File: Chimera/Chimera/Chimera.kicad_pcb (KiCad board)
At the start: 4 copper layers, 72 x 41.5 mm, 110 parts, among them J1 Fork 1, J10 DM3CS-SF, J2 Fork 2, J3 Flamethrower, J4 Therm 1, J5 Therm 2, J6 Therm 3, J7 Therm 4, J8 Button, J9 USB_B_Micro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

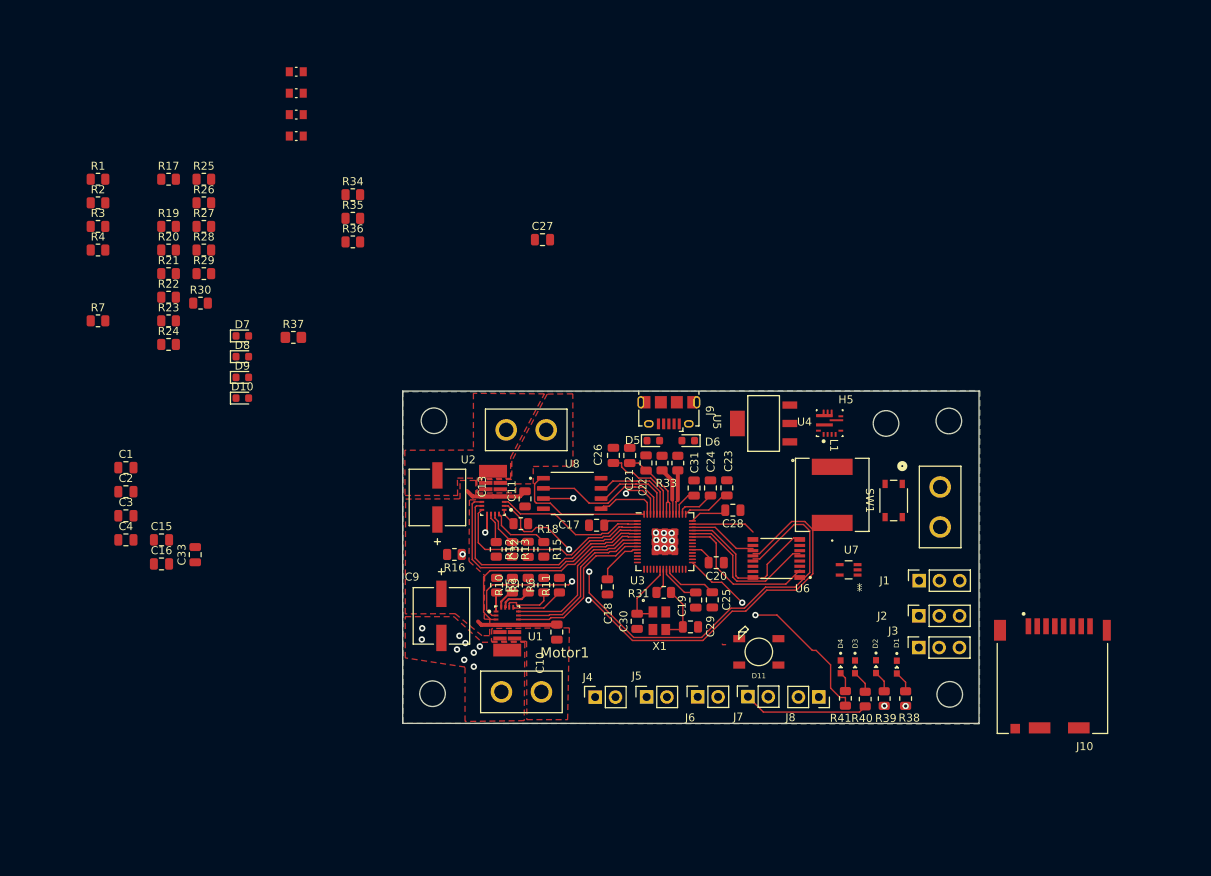
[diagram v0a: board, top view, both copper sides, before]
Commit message: Rewiring M2 and moved Debugging LEDS
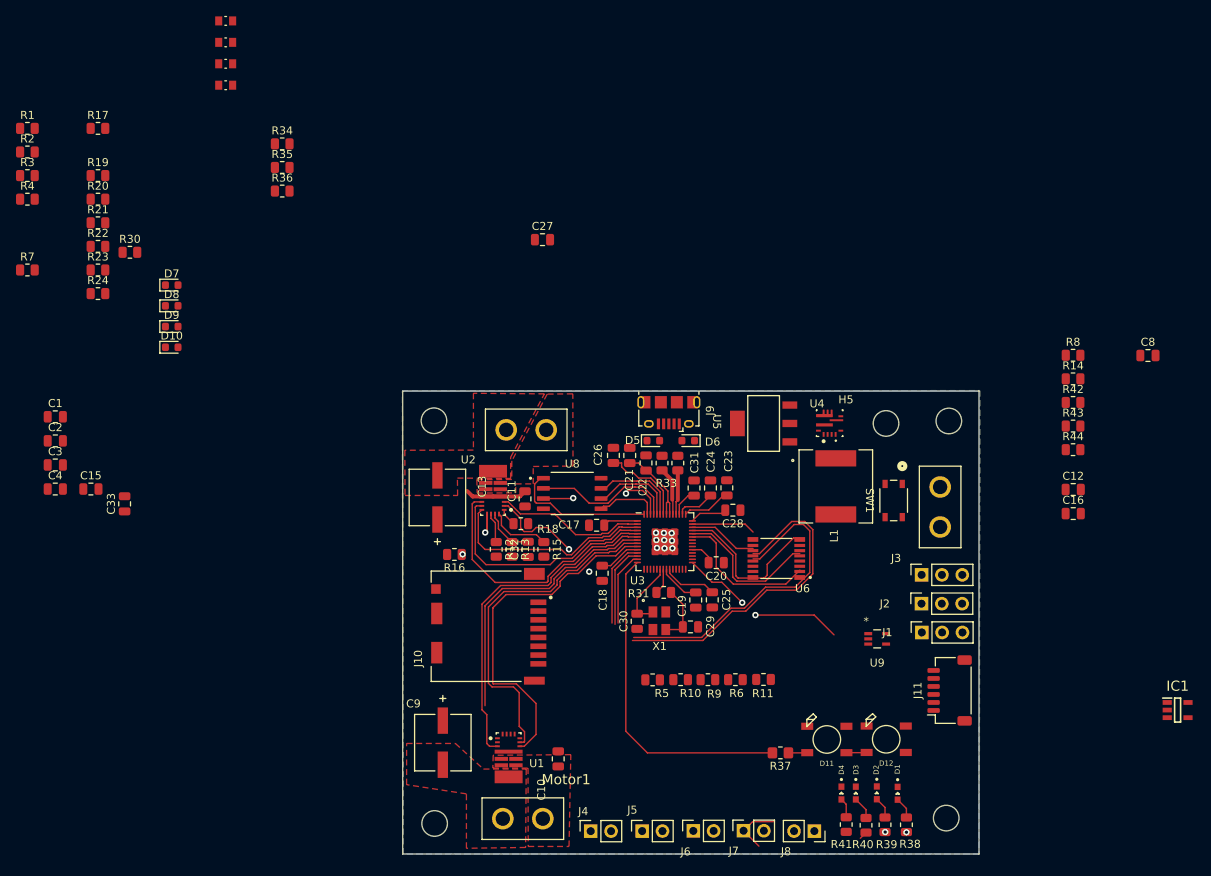
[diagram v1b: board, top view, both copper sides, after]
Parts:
- removed R25: 100m, Resistor_SMD:R_0805_2012Metric
- removed R26, R27: 10k, Resistor_SMD:R_0805_2012Metric
- removed R28, R29: 500k, Resistor_SMD:R_0805_2012Metric
- removed U7: OpAmp, chimera:SC70-5_LT_MCH-M
- added C12: 1uF, Capacitor_SMD:C_0805_2012Metric, F.Cu at (155.7, 74.0)
- added C8: .1uF, Capacitor_SMD:C_0805_2012Metric, F.Cu at (165.0, 57.3)
- added D12: NeoPixel_THT, chimera:WS2812B, F.Cu at (132.3, 105.2)
- added IC1: AP7375-50W5-7, chimera:SOT95P285X140-5N, F.Cu at (168.7, 101.6)
- added J11: Reciver, Connector_JST:JST_SH_SM06B-SRSS-TB_1x06-1MP_P1.00mm_Horizontal, F.Cu at (140.2, 99.1)
- added R14: 10k, Resistor_SMD:R_0805_2012Metric, F.Cu at (155.7, 60.2)
- added R42: 10k, Resistor_SMD:R_0805_2012Metric, F.Cu at (155.7, 63.1)
- added R43: 500k, Resistor_SMD:R_0805_2012Metric, F.Cu at (155.7, 66.1)
- added R44: 500k, Resistor_SMD:R_0805_2012Metric, F.Cu at (155.7, 69.0)
- added R8: 100m, Resistor_SMD:R_0805_2012Metric, F.Cu at (155.7, 57.2)
- added U9: OpAmp, chimera:SC70-5_LT_MCH-M, F.Cu at (131.2, 92.7)
- C16: value .1uF -> 10uF
- moved C16 114.1 mm to (155.7, 77.0)
- moved R37 80.0 mm to (119.1, 106.9), turned to 180 degrees
- moved J10 71.1 mm to (82.5, 91.3), turned to 90 degrees
- moved R11 28.1 mm to (117.0, 97.8), turned to 0 degrees
- moved R6 26.7 mm to (113.5, 97.8), turned to 0 degrees
- moved R9 25.4 mm to (110.0, 97.8), turned to 0 degrees
- moved R10 24.1 mm to (106.6, 97.8), turned to 0 degrees
- moved R5 22.8 mm to (103.1, 97.8), turned to 0 degrees
- moved J4 16.8 mm to (95.4, 116.7)
- moved J5 16.8 mm to (101.8, 116.7)
- moved J6 16.8 mm to (108.2, 116.7)
- moved J7 16.8 mm to (114.5, 116.7)
- moved J8 16.8 mm to (123.3, 116.7)
- moved H3 16.2 mm to (75.9, 115.8)
- moved C9 15.9 mm to (76.9, 105.7)
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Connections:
- net /Servo_Current_Sense renamed Servo_Current_Sense
- C16 pad 2: +3.3V -> +5V
- D11 pad 1: unconnected-(D11-DOUT-Pad1) -> Net-(D11-DOUT)
- U3 pad 31: unconnected-(U3-GPIO20-Pad31) -> /MCU/Transmitter-MCU_TX
- U3 pad 32: unconnected-(U3-GPIO21-Pad32) -> /MCU/Transmitter-MCU_RX
- U6 pad 10: /Current_Sense -> Current_Sense
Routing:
- net /IPROPI1: track 67.1 -> 0.00 mm, vias 2 -> 0
- net /MCU/NEO: track 0.00 -> 41.1 mm
- net IPROPI1/2: track 8.68 -> 49.8 mm
- net DRVOFF1: track 20.8 -> 44.1 mm
- net EN_IN1: track 20.8 -> 43.2 mm
- net Sleep_1: track 27.7 -> 42.5 mm
- net PH_IN1: track 20.7 -> 35.3 mm
- net Fork1: track 0.00 -> 10.8 mm
- net IPROPI2: track 65.8 -> 55.3 mm
- net Fork2: track 0.00 -> 10.3 mm
- net +BATT: track 17.8 -> 7.77 mm
- net Flame_Servo: track 0.00 -> 9.27 mm
- net +3.3V: track 60.7 -> 52.1 mm
- net /MCU/LED: track 29.3 -> 21.9 mm
- net Net-(U1-DIAG): track 6.62 -> 0.00 mm
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- removed copper zone on F.Cu, net +BATT
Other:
- board size 72 x 41.5 mm -> 72 x 57.9 mm

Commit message: added reciever and fixed wiring below MCU
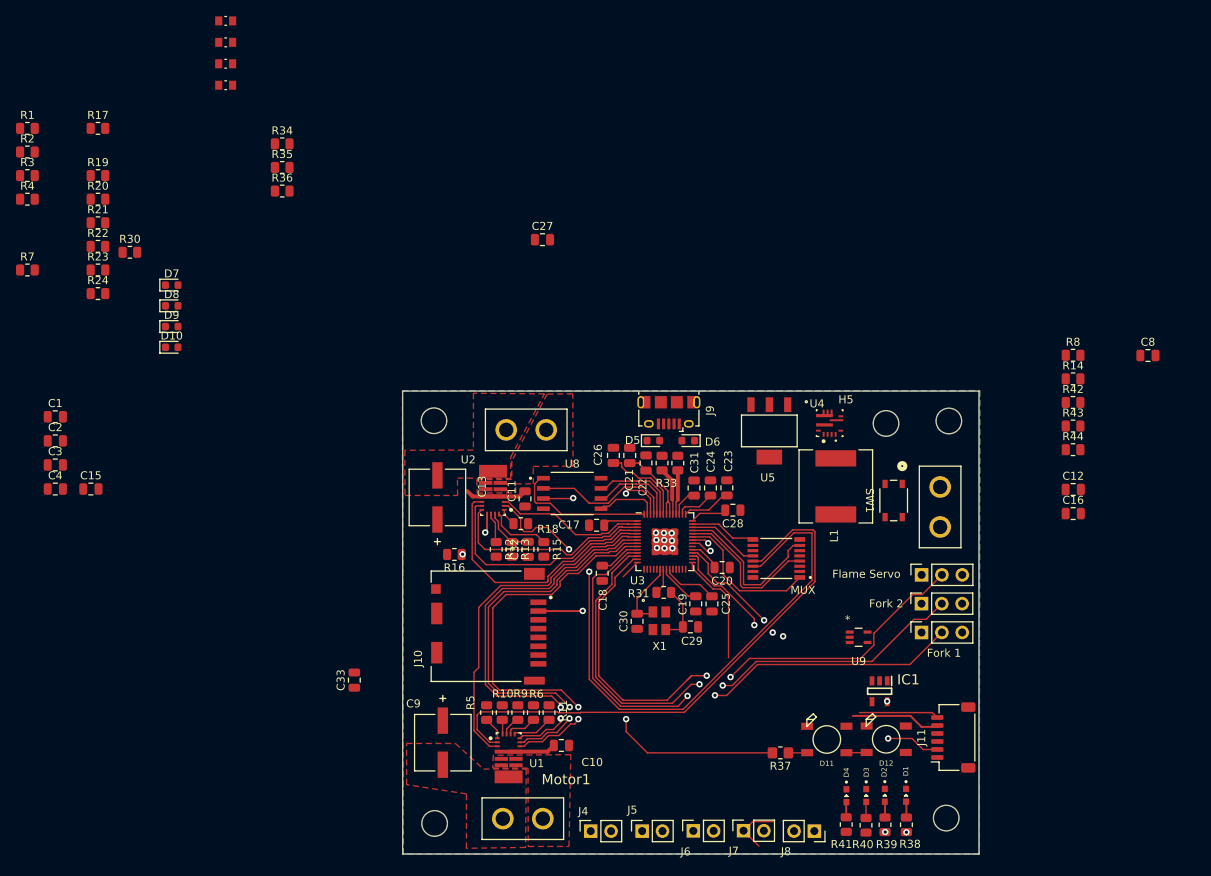
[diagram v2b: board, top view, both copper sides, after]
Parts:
- Flame Servo: renamed from J3
- Fork 1: renamed from J1
- Fork 2: renamed from J2
- moved IC1 37.3 mm to (131.5, 99.2), turned to -90 degrees
- moved C33 36.2 mm to (65.8, 97.8)
- moved R11 27.1 mm to (90.2, 101.9), turned to 90 degrees
- moved R6 25.6 mm to (88.2, 101.9), turned to 90 degrees
- moved R9 24.1 mm to (86.3, 101.9), turned to 90 degrees
- moved R10 22.7 mm to (84.3, 101.9), turned to 90 degrees
- moved R5 21.1 mm to (82.4, 101.9), turned to -90 degrees
- moved J11 5.90 mm to (140.7, 105.0)
- moved U9 2.33 mm to (128.9, 92.5)
- moved C10 1.72 mm to (91.7, 106.0), turned to 180 degrees
- moved D3 1.33 mm to (129.8, 112.3)
- moved U5 1.17 mm to (117.7, 66.7), turned to 180 degrees
- moved D1 1.08 mm to (134.8, 112.2)
- moved D2 1.04 mm to (132.1, 112.2)
- moved C20 0.96 mm to (111.8, 83.8)
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- renumbered U6 to MUX
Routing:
- net /IPROPI1: track 0.00 -> 70.0 mm
- net Flame_Servo: track 9.27 -> 69.5 mm, vias 0 -> 2
- net Fork1: track 10.8 -> 68.6 mm, vias 0 -> 2
- net Fork2: track 10.3 -> 67.8 mm, vias 0 -> 2
- net IPROPI1/2: track 49.8 -> 9.05 mm
- net /MCU/Transmitter-MCU_TX: track 0.00 -> 27.1 mm, vias 0 -> 2
- net /MCU/Transmitter-MCU_RX: track 0.00 -> 26.2 mm, vias 0 -> 2
- net IPROPI2: track 55.3 -> 80.0 mm
- net PH_IN1: track 35.3 -> 51.6 mm, vias 0 -> 2
- net /MCU/NEO: track 41.1 -> 25.5 mm, vias 0 -> 1
- net +5V: track 0.00 -> 11.4 mm, vias 0 -> 2
- net DRVOFF1: track 44.1 -> 53.5 mm, vias 0 -> 2
- net EN_IN1: track 43.2 -> 52.4 mm, vias 0 -> 2
- net /MCU/LED: track 21.9 -> 14.3 mm, vias 2 -> 0
- net +BATT: track 7.77 -> 13.7 mm
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
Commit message: Saving changes, to revert and look at previous routing
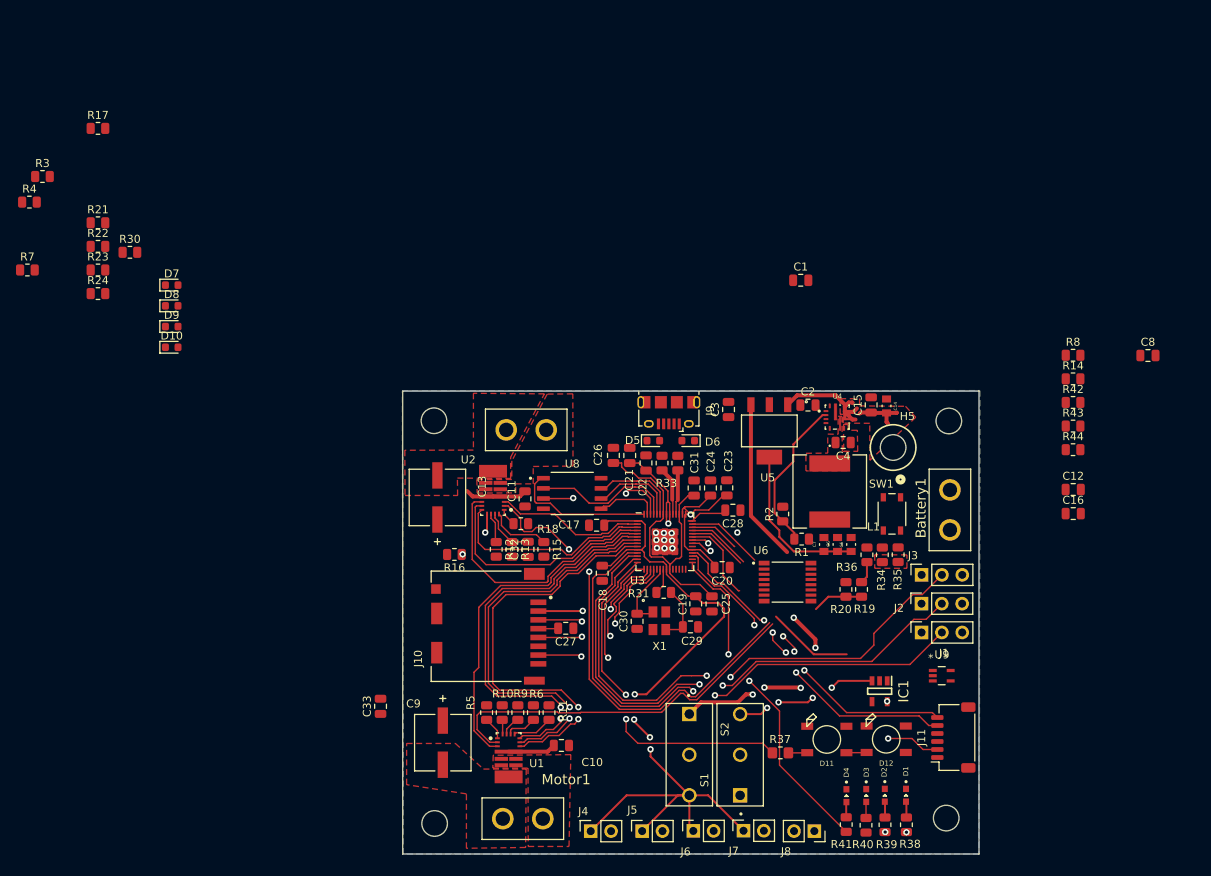
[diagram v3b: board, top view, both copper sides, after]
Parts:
- added S1: D2F-01F, rocketry_footprints:SW_D2F-01F, F.Cu at (114.0, 107.2)
- added S2: D2F-01F, rocketry_footprints:SW_D2F-01F, F.Cu at (107.7, 107.2)
- J1: renamed from Fork 1
- J2: renamed from Fork 2
- J3: renamed from Flame Servo
- U4: footprint chimera:RPA0010A-MFG -> chimera:CONV_TPS56837RPAR
- moved R1 109.6 mm to (121.7, 80.2), turned to 180 degrees
- moved R19 108.6 mm to (129.2, 86.5), turned to -90 degrees
- moved R20 105.5 mm to (127.3, 86.5), turned to 90 degrees
- moved R2 104.7 mm to (119.4, 77.1), turned to 90 degrees
- moved C5 102.0 mm to (127.9, 80.9), turned to 90 degrees
- moved C6 98.9 mm to (126.2, 80.9), turned to 90 degrees
- moved C4 98.7 mm to (126.9, 68.2), turned to 180 degrees
- moved C15 98.1 mm to (130.4, 63.5), turned to -90 degrees
- moved C7 95.9 mm to (124.5, 80.9), turned to 90 degrees
- moved C1 94.7 mm to (121.6, 47.9)
- moved C2 94.2 mm to (122.5, 63.5)
- moved C14 91.8 mm to (132.3, 63.6), turned to -90 degrees
- moved R35 90.9 mm to (133.8, 82.2), turned to 90 degrees
- moved R34 90.9 mm to (131.8, 82.2), turned to -90 degrees
- moved R36 86.1 mm to (129.9, 82.2), turned to 90 degrees
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- renumbered MUX to U6
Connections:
- C3 pad 2: +3.3V -> Net-(U5-OUTPUT)
- IC1 pad 3: +BATT -> Net-(IC1-EN)
- U5 pad 3: +3.3V -> Net-(U5-OUTPUT)
- U6 pad 10: Current_Sense -> /V_Bat_Mon
- U6 pad 11: /V_Bat_Mon -> Current_Sense
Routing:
- net +3.3V: track 52.1 -> 142.2 mm, vias 0 -> 6
- net Net-(U5-OUTPUT): track 0.00 -> 46.9 mm, vias 0 -> 5
- net /MCU/LED: track 14.3 -> 42.2 mm, vias 0 -> 2
- net /MCU/SD_MISO: track 0.00 -> 22.7 mm, vias 0 -> 2
- net +BATT: track 13.7 -> 36.3 mm
- net /IPROPI1: track 70.0 -> 47.4 mm
- net IPROPI2: track 80.0 -> 58.2 mm
- net /MCU/SD CK: track 0.00 -> 21.1 mm, vias 0 -> 2
- net GND: track 0.00 -> 20.2 mm
- net /MCU/SD_MOSI: track 0.00 -> 19.7 mm, vias 0 -> 2
- net Net-(U4-FB): track 0.00 -> 19.4 mm
- net Net-(IC1-EN): track 0.00 -> 18.8 mm, vias 0 -> 4
- net /MCU/NEO: track 25.5 -> 43.8 mm, vias 1 -> 2
- net Net-(U3-VREG_VOUT): track 21.4 -> 38.5 mm
- net /MCU/Transmitter-MCU_RX: track 26.2 -> 42.3 mm, vias 2 -> 4
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- added copper zone on In2.Cu, net +7.5V
- added copper zone on B.Cu, net +BATT
- added copper zone on F.Cu, net +BATT
- added copper zone on F.Cu, net Net-(R34-Pad2)
- added copper zone on F.Cu, net Net-(U4-BOOT)
- added copper zone on F.Cu, net Net-(U4-SW)
- removed copper zone on B.Cu, net +7.5V
- removed copper zone on In2.Cu, net +BATT

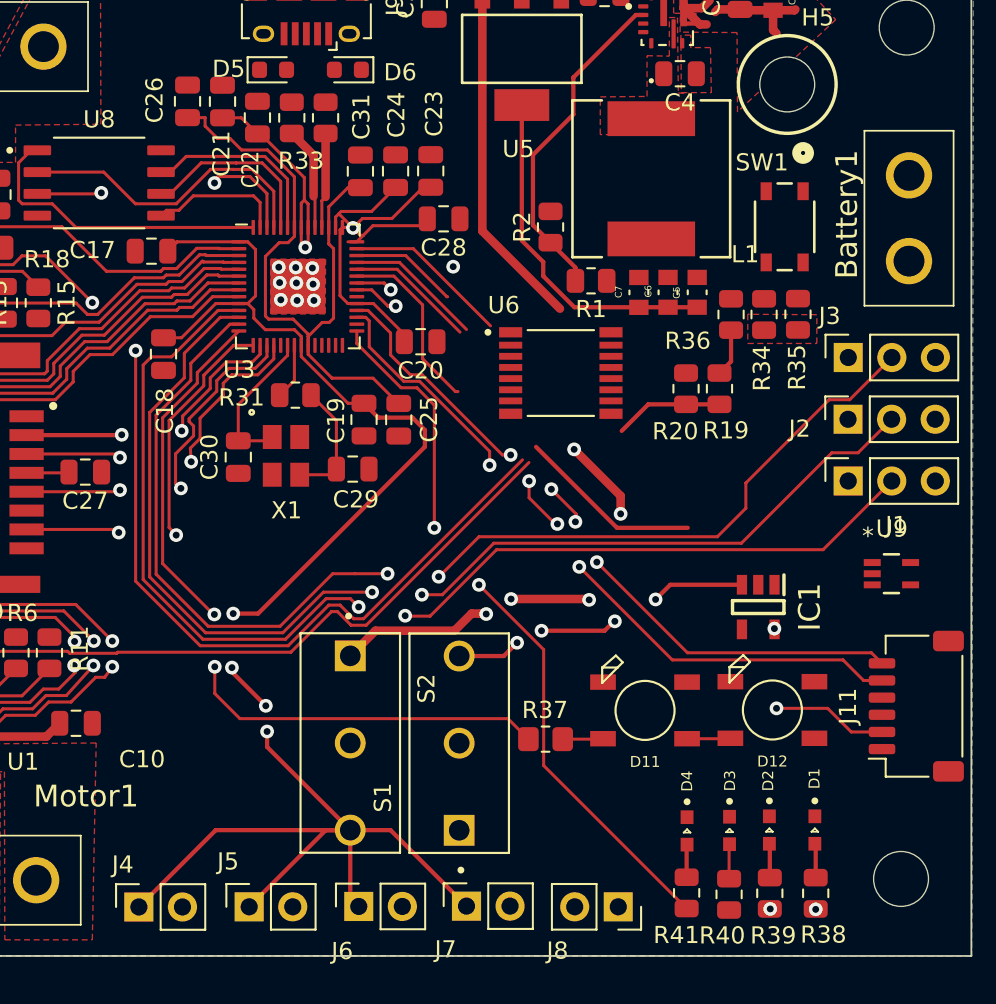
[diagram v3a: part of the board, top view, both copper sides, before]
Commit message: Fixed roughting on MUX, some minor details left for thermistor traces
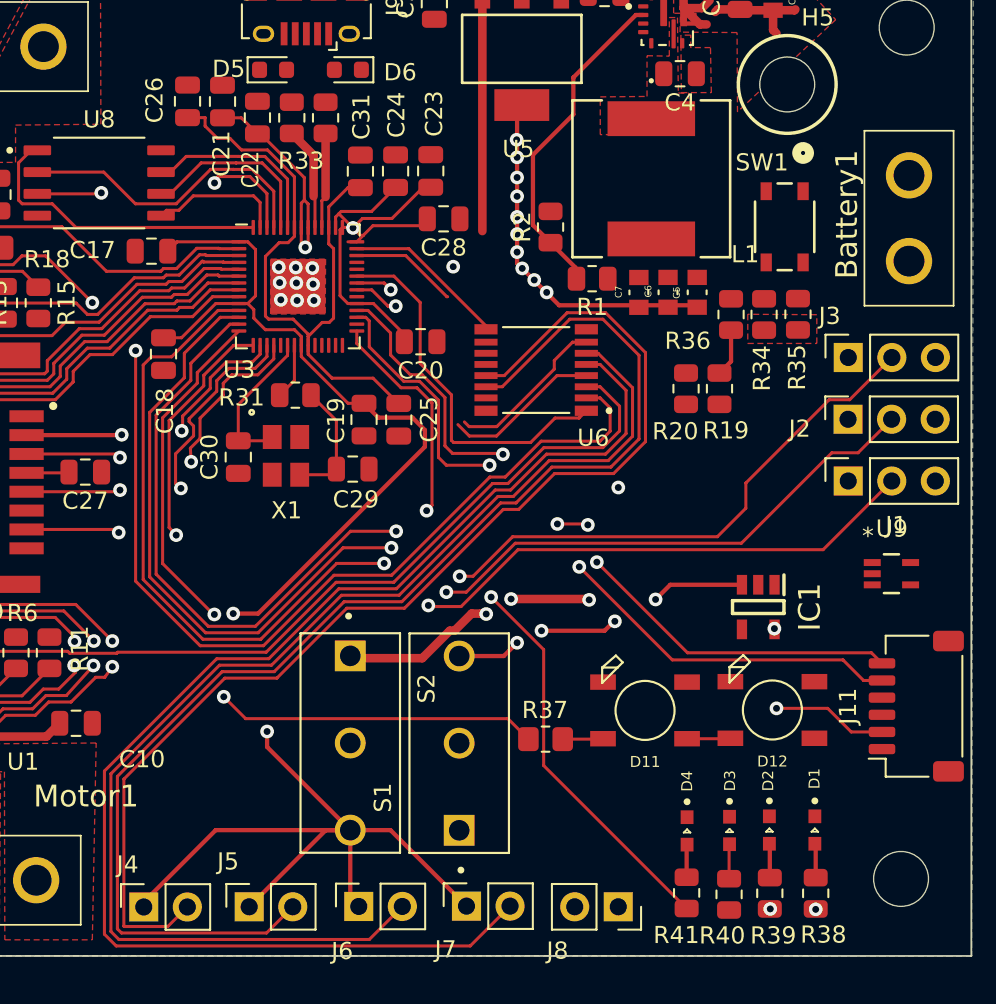
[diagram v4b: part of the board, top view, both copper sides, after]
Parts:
- moved U6 1.45 mm to (118.5, 85.4), turned to 180 degrees
- moved J4 0.28 mm to (95.7, 116.7)
- moved R1 0.14 mm to (121.8, 80.1)
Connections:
- U3 pad 38: Therm1/2 -> Therm3/4
- U3 pad 39: Therm3/4 -> Therm1/2
- U6 pad 10: /V_Bat_Mon -> Current_Sense
- U6 pad 11: Current_Sense -> /V_Bat_Mon
- U6 pad 12: IPROPI1/2 -> Therm1/2
- U6 pad 13: /IPROPI1 -> /Therm1
- U6 pad 14: IPROPI2 -> /Therm2
- U6 pad 2: /Therm1 -> IPROPI2
- U6 pad 3: /Therm2 -> /IPROPI1
- U6 pad 4: Therm1/2 -> IPROPI1/2
- U6 pad 5: /Therm3 -> /Therm4
- U6 pad 6: /Therm4 -> /Therm3
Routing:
- net /Therm4: track 0.00 -> 78.4 mm
- net /Therm2: track 0.00 -> 74.7 mm
- net /Therm3: track 0.00 -> 72.1 mm
- net /Therm1: track 0.00 -> 68.3 mm
- net MUX_Select: track 10.5 -> 21.8 mm
- net Current_Sense: track 10.8 -> 0.00 mm
- net Net-(U5-OUTPUT): track 46.9 -> 37.3 mm, vias 5 -> 4
- net /IPROPI1: track 47.4 -> 56.7 mm
- net IPROPI1/2: track 6.29 -> 15.5 mm
- net IPROPI2: track 58.2 -> 66.3 mm
- net Therm1/2: track 7.54 -> 0.00 mm
- net /V_Bat_Mon: track 6.34 -> 0.00 mm
- net /MCU/Transmitter-MCU_RX: track 42.3 -> 46.7 mm
- net Flame_Servo: track 68.7 -> 70.9 mm
- net Fork2: track 67.8 -> 69.8 mm
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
